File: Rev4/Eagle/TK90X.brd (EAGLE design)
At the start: 217.8 x 132.1 mm, 222 parts, among them IC1 Z80, IC10 74LS365N, IC11 LM1886, IC12 LM1889, IC13 4116, IC14 4116, IC15 4116, IC16 4116, IC17 4116, IC18 4116, IC19 4116, IC2 ROM, IC20 4116, IC21 4416, IC22 4416, IC23 4416, IC24 4416, IC25 74LS00, IC26 74LS00, IC27 74LS32, IC28 74LS04, IC3 ULA TK90, IC4 74LS74, IC5 74LS74, IC6 74LS157, IC7 74LS157, IC8 74LS157, IC9 74LS157, J1 0R-JUMPB, J2 0R-JUMPB, Q1 BC548, Q2 BC548, Q3 BF494, Q4 BC548, Q5 BD139, Q6 BD136, Q7 BC548, Q8 BC517, X1 RCA2PINA1, X2 POWER

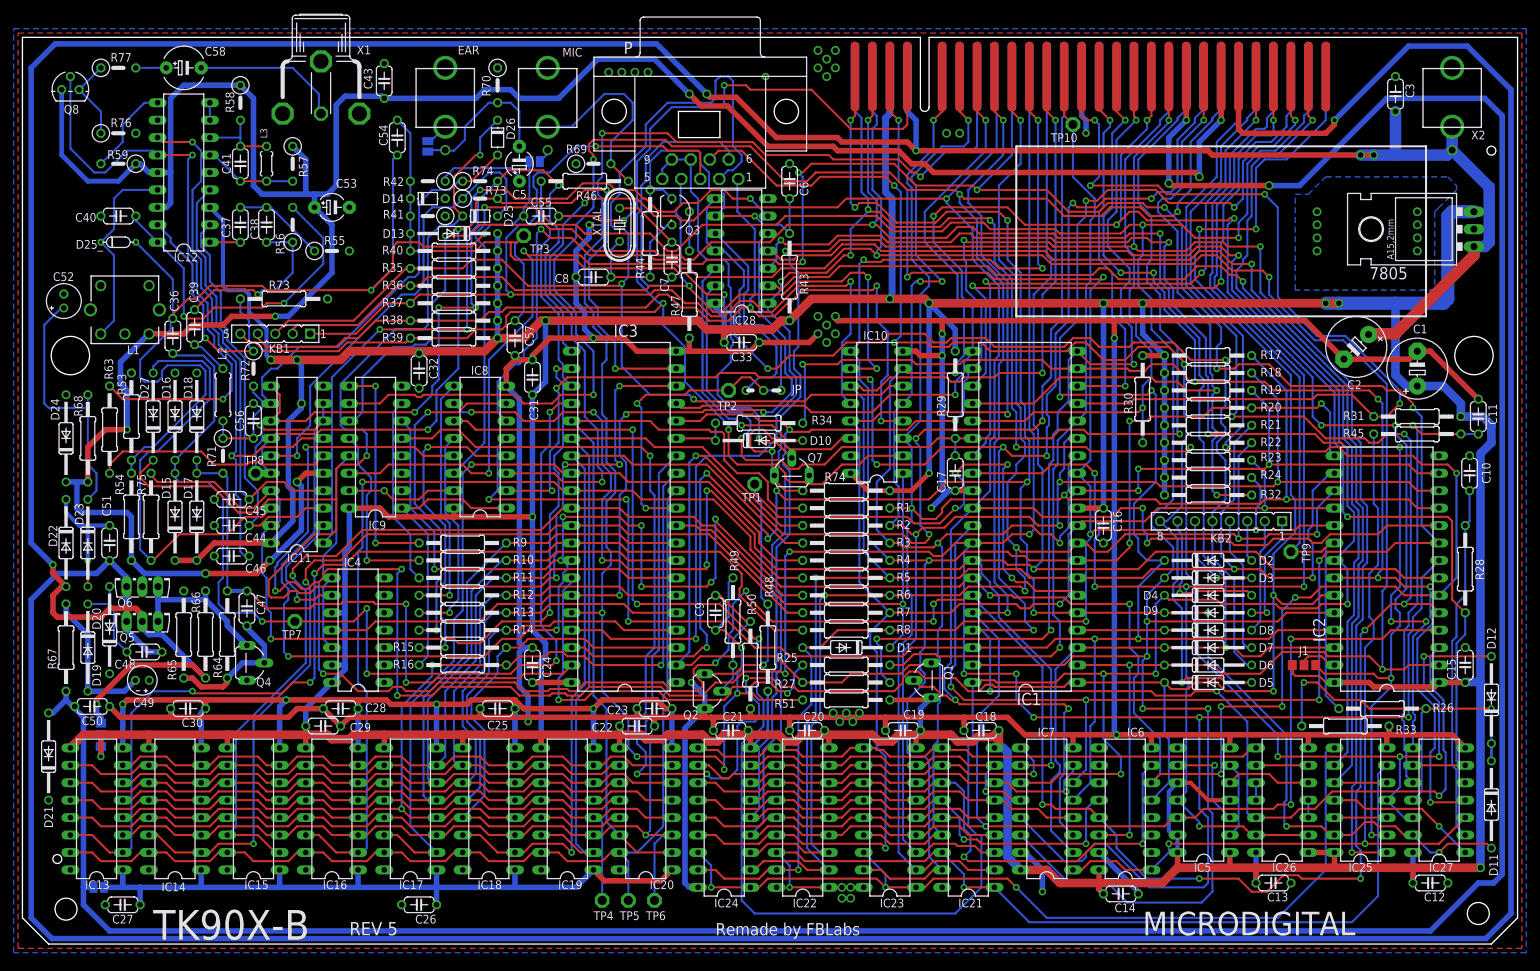
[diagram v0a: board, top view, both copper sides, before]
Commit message: Corrigido conexões power Adicionado jumpers de solda pros jacks de áudio Adicionado revisão 6 com 74LS365 substituido pelo 74LS244
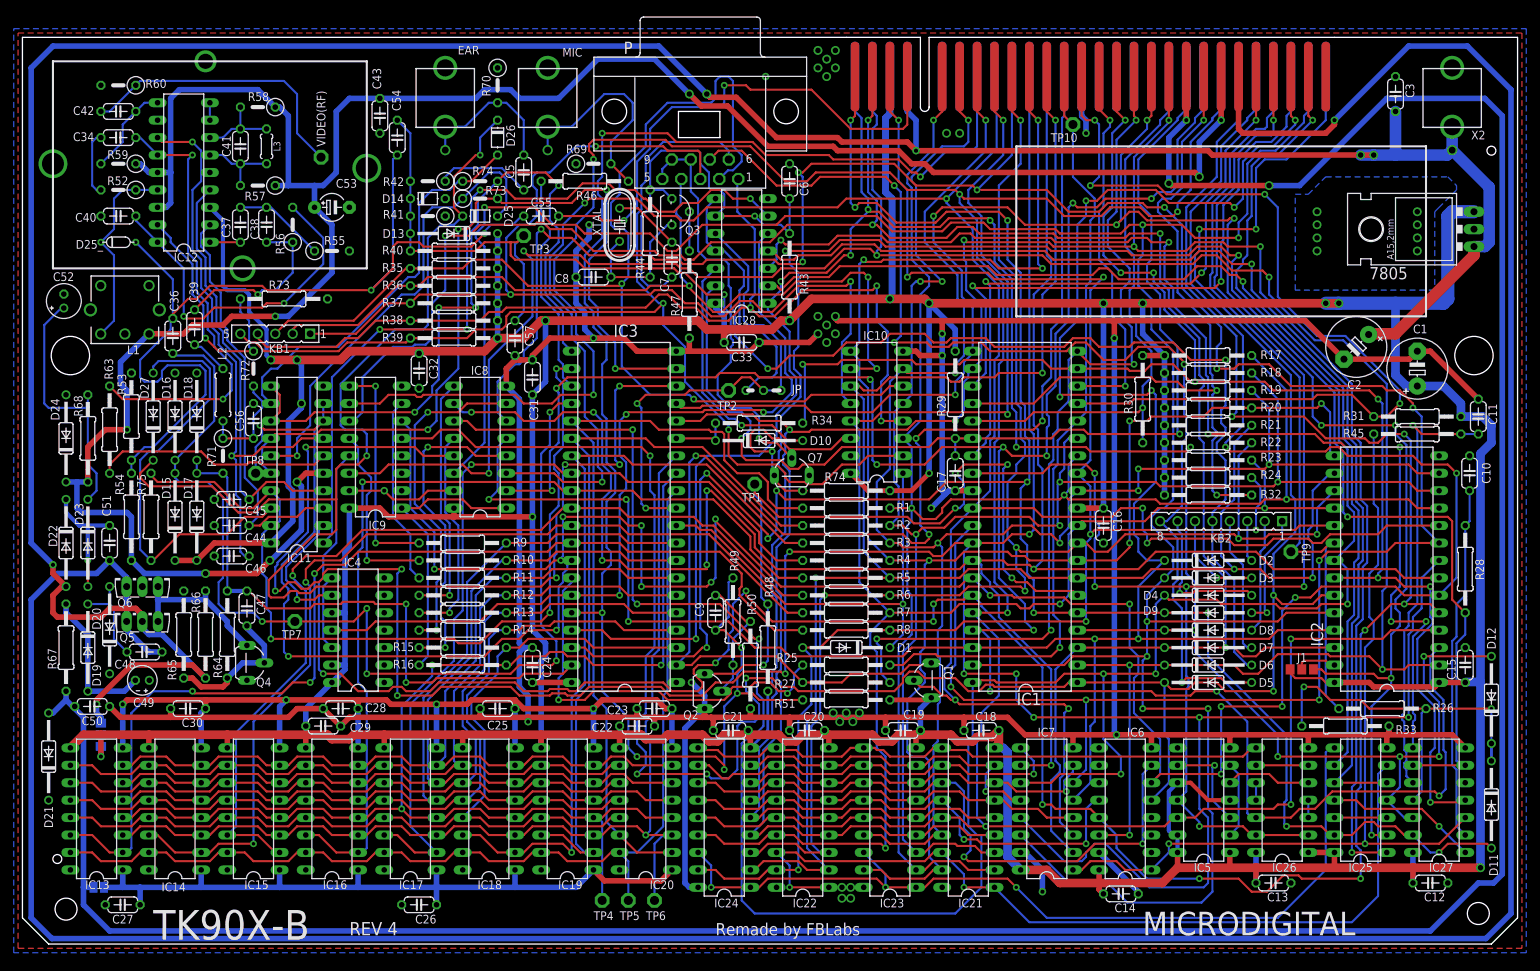
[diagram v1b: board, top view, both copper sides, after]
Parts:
- removed C58: 220u, rcl:E5-6
- removed J4, J5: (no value), jumper:SJ
- removed Q8: BC517, transistor-npn:TO92
- removed R76: 150, rcl:0207/5V
- removed R77: 75, rcl:0207/5V
- removed X1: RCA2PINA1, tk90:TOBU3
- added C34: 47p, rcl:C050-024X044
- added C42: 100n, rcl:C050-024X044
- added R52: 22K, rcl:0207/5V
- added R60: ?, rcl:0207/5V
- added VIDEO(RF): RF, testpad:P1-13
- C5: value 100u -> 100n; device rcl:E5-4 -> rcl:C050-024X044
- moved R57 5.99 mm to (34.3, 110.5), turned to 180 degrees
- moved C43 5.12 mm to (52.1, 120.7), turned to 90 degrees
- moved R58 2.62 mm to (34.3, 121.9), turned to 180 degrees
- moved C41 2.54 mm to (31.8, 116.2)
- moved L3 2.54 mm to (35.6, 116.2)
- moved C5 1.42 mm to (73.0, 112.4)
- moved J1 0.71 mm to (186.4, 40.0)
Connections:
- removed net AUDIO: C36.2, C54.2, C55.1, D25_.A, J4.1, R53.1, R54.2
- removed net N$48 (its old number): Q8.1, R76.1, R77.1
- removed net N$88: EAR.NC, J5.2
- net +12V: no longer Q8.3
- net GND: now also R60.2; no longer R76.2, X1.SHELL, X1.SHELL@1, X1.SHELL@2
- net N$16: now also C5.2, EAR.NC; no longer C5.-, J5.1
- net N$44: now also MIC.TIP
- net N$50: now also C36.2, C54.2, C55.1, D25_.A, R53.1, R54.2; no longer J4.2, MIC.TIP
- net N$69: now also C34.1; no longer Q8.2
- net N$73: now also C42.1
- net N$74: now also C42.2, R60.1, VIDEO(RF).1; no longer C58.-, X1.PIN
- net N$75: now also R52.1
- net N$76: now also C34.2, R52.2; no longer C58.+, R77.2
- net N$9: now also C5.1; no longer C5.+
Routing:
- net AUDIO: track 146.0 -> 0.00 mm, vias 2 -> 0
- net N$50: track 2.14 -> 137.7 mm, vias 0 -> 2
- net +12V: track 390.1 -> 357.5 mm
- net N$69: track 87.6 -> 65.6 mm
- net N$74: track 21.7 -> 41.9 mm
- net N$48 (its old number): track 12.2 -> 0.00 mm
- net N$76: track 4.44 -> 9.42 mm
- net N$44: track 28.7 -> 32.1 mm
- net N$88: track 3.41 -> 0.00 mm
- net N$87: track 13.6 -> 12.0 mm
- net N$10: track 59.6 -> 58.8 mm
- net N$9: track 13.1 -> 13.9 mm
- net N$16: track 23.1 -> 22.4 mm
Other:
- board text added: "REV 4"
- board text removed: "REV 5"
